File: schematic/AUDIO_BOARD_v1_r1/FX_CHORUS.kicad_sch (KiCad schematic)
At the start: 43 parts, among them U70 MN3207, U71 MN3207, U72 MN3101, U73 OPA1678, U74 OPA1678, U75 OPA1678, U76 4053, U77 OPA1678

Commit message: SIM and trying to figure out stackup/placement
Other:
- moved on the sheet: C1053, C1055, C1056, C1060, C1064, C1070, C1074, C1085, C1086, C1087, C1088, C1089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

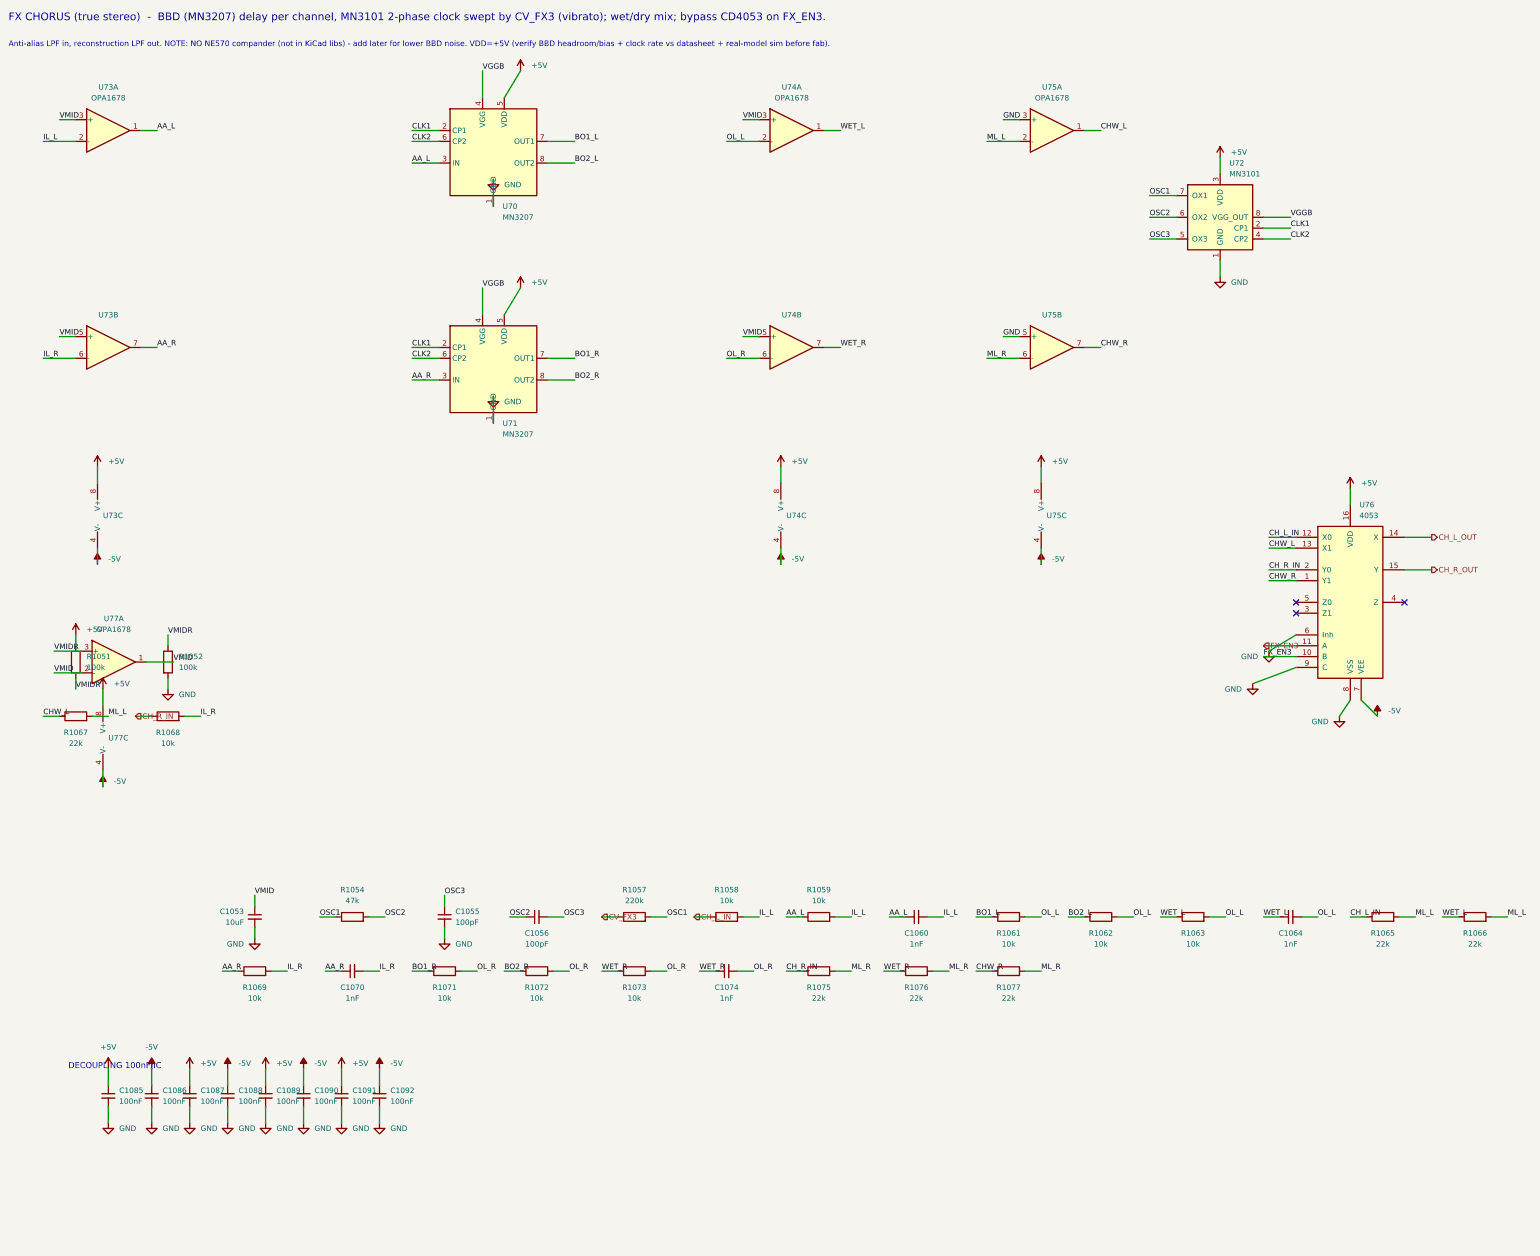
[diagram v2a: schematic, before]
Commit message: more placement and routing
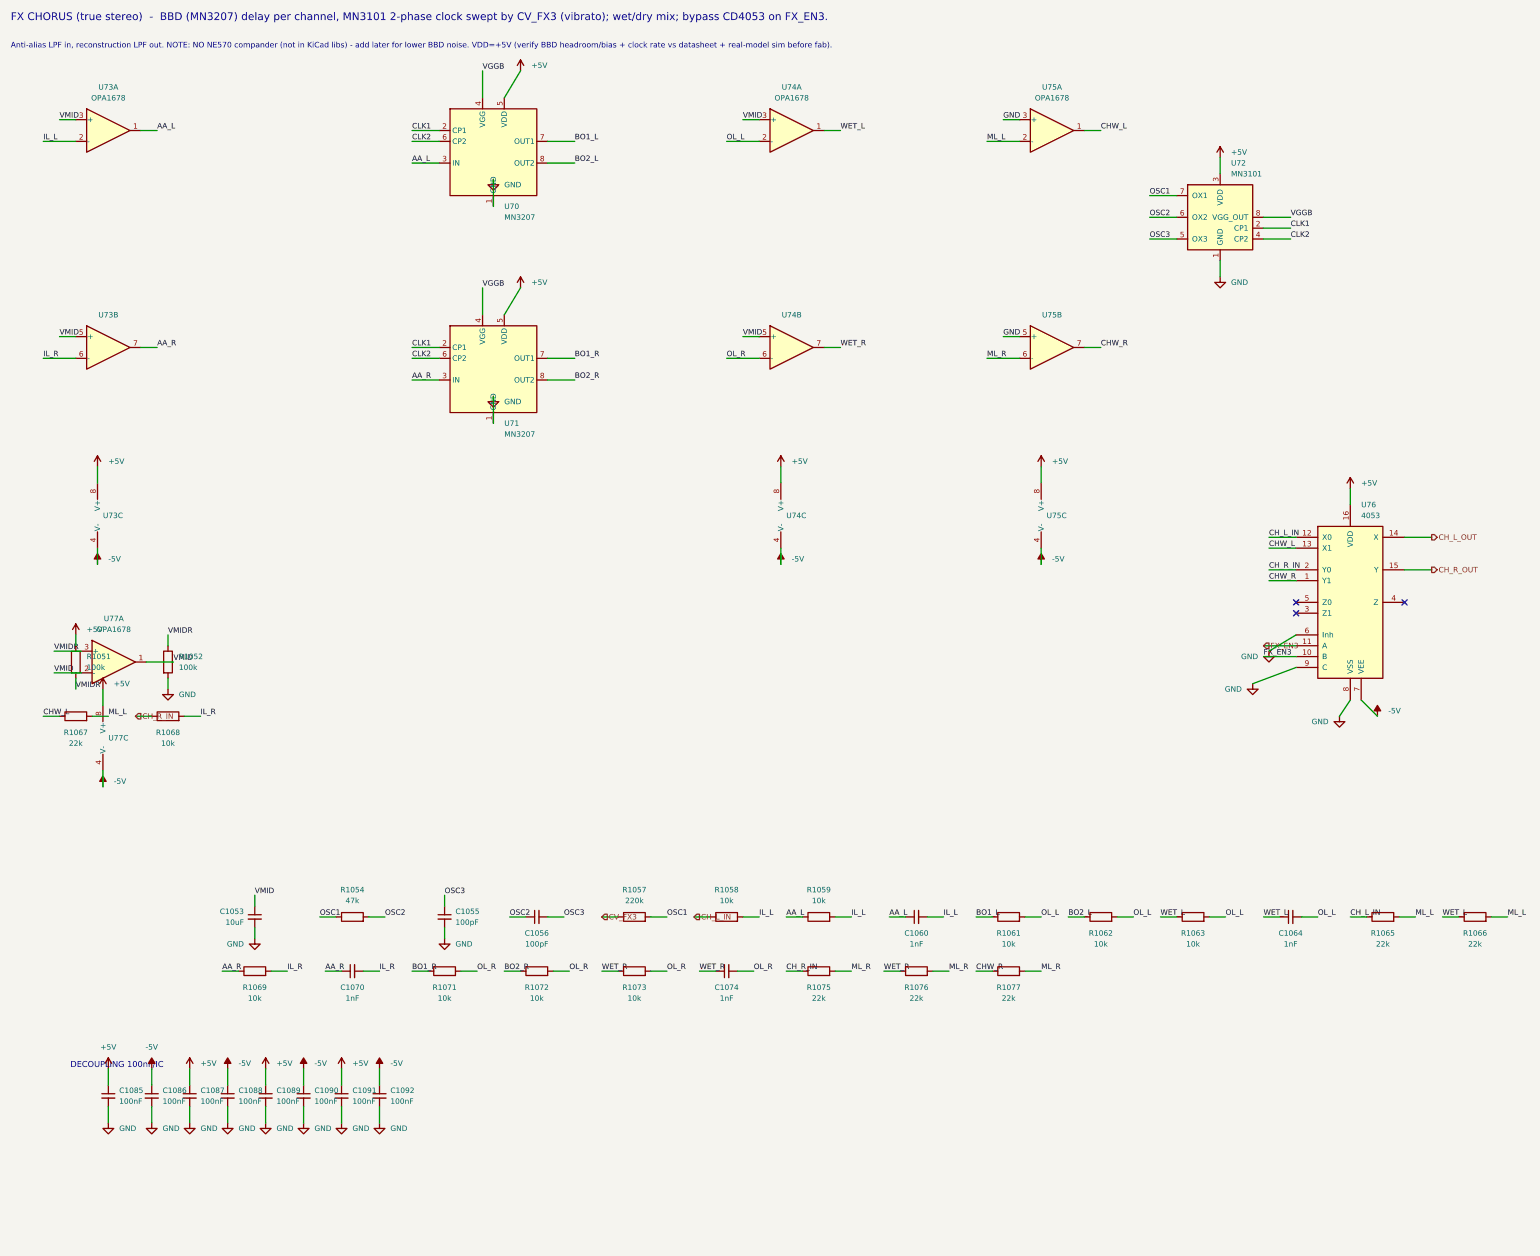
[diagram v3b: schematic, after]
